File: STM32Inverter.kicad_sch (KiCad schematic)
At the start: 99 parts, among them J1 STLINK, J2 CURRENT SENSE, J5 UART, J6 INTERFACE, J7 POWER, J8 501571-2007, J9 RESOLVER, Q4 ST3422A, U1 STM32F303VCTx, U10 ULN2002, U11 LM393, U12 LM393, U4 74HCT00, U7 MCP2551-I-SN, Y3 CSTNE8M00GH5C000R0

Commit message: Review done
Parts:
- added JP1, JP2: ~, MEMS_Passive:R_0805_2012Metric_Jumper, symbol MEMS_Passive:SolderableJumper
- added unit 3 of U4
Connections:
- net GND: now also JP1.2, JP2.2, U4.10, U4.9
- net at J6.12, JP2.2: now also JP1.1
- net at J6.14, JP1.2: now also JP2.1
- no-connect marks 5 -> 53
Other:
- note removed: "CHECK NTC TEMP RANGE"
- note removed: "CHECK PINOUT"
- note removed: "Zrob Cos z VBUSEM !!!!"
- moved on the sheet: F3, JP1, JP2

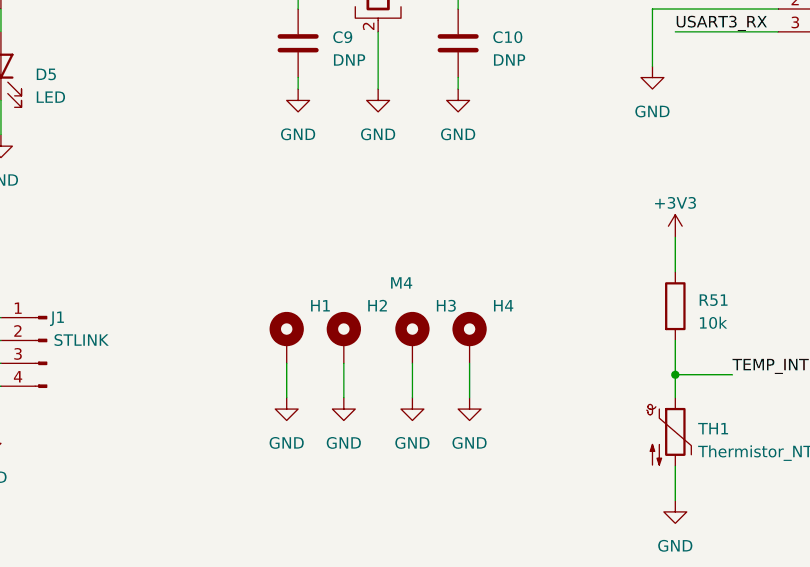
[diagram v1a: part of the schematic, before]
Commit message: change holes
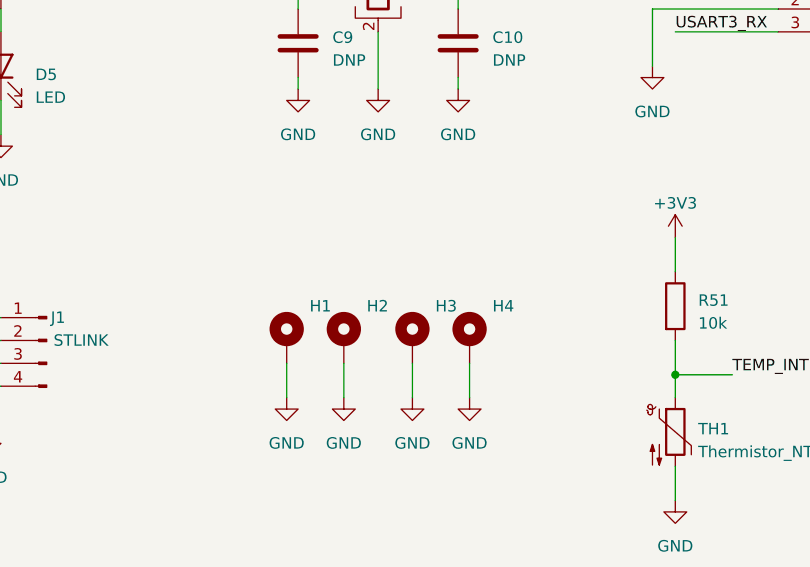
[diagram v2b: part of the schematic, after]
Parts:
- H1: value M4 -> MountingHole_Pad; footprint MountingHole:MountingHole_4.3mm_M4_ISO7380_Pad -> MountingHole:MountingHole_4.3mm_M4_Pad_Via
- H2, H3, H4: footprint MountingHole:MountingHole_4.3mm_M4_ISO7380_Pad -> MountingHole:MountingHole_4.3mm_M4_Pad_Via
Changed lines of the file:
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@@
       (effects (font (size 1.27 1.27)) (justify left) hide)
     )
-    (property "Footprint" "MountingHole:MountingHole_4.3mm_M4_ISO7380_Pad" (at 256.54 367.03 0)
+    (property "Footprint" "MountingHole:MountingHole_4.3mm_M4_Pad_Via" (at 256.54 367.03 0)
       (effects (font (size 1.27 1.27)) hide)
     )
@@
       (effects (font (size 1.27 1.27)) (justify left) hide)
     )
-    (property "Footprint" "MountingHole:MountingHole_4.3mm_M4_ISO7380_Pad" (at 250.19 367.03 0)
+    (property "Footprint" "MountingHole:MountingHole_4.3mm_M4_Pad_Via" (at 250.19 367.03 0)
       (effects (font (size 1.27 1.27)) hide)
     )
@@
       (effects (font (size 1.27 1.27)) (justify left) hide)
     )
-    (property "Footprint" "MountingHole:MountingHole_4.3mm_M4_ISO7380_Pad" (at 242.57 367.03 0)
+    (property "Footprint" "MountingHole:MountingHole_4.3mm_M4_Pad_Via" (at 242.57 367.03 0)
       (effects (font (size 1.27 1.27)) hide)
     )
@@
       (effects (font (size 1.27 1.27)) (justify left))
     )
-    (property "Value" "M4" (at 247.65 360.68 0)
-      (effects (font (size 1.27 1.27)) (justify left))
-    )
-    (property "Footprint" "MountingHole:MountingHole_4.3mm_M4_ISO7380_Pad" (at 236.22 367.03 0)
-      (effects (font (size 1.27 1.27)) hide)
-    )
+    (property "Value" "MountingHole_Pad" (at 240.03 360.68 0)
+      (effects (font (size 1.27 1.27)) (justify left) hide)
+    )
+    (property "Footprint" "MountingHole:MountingHole_4.3mm_M4_Pad_Via" (at 236.22 367.03 0)
+      (effects (font (size 1.27 1.27)) hide)
+    )

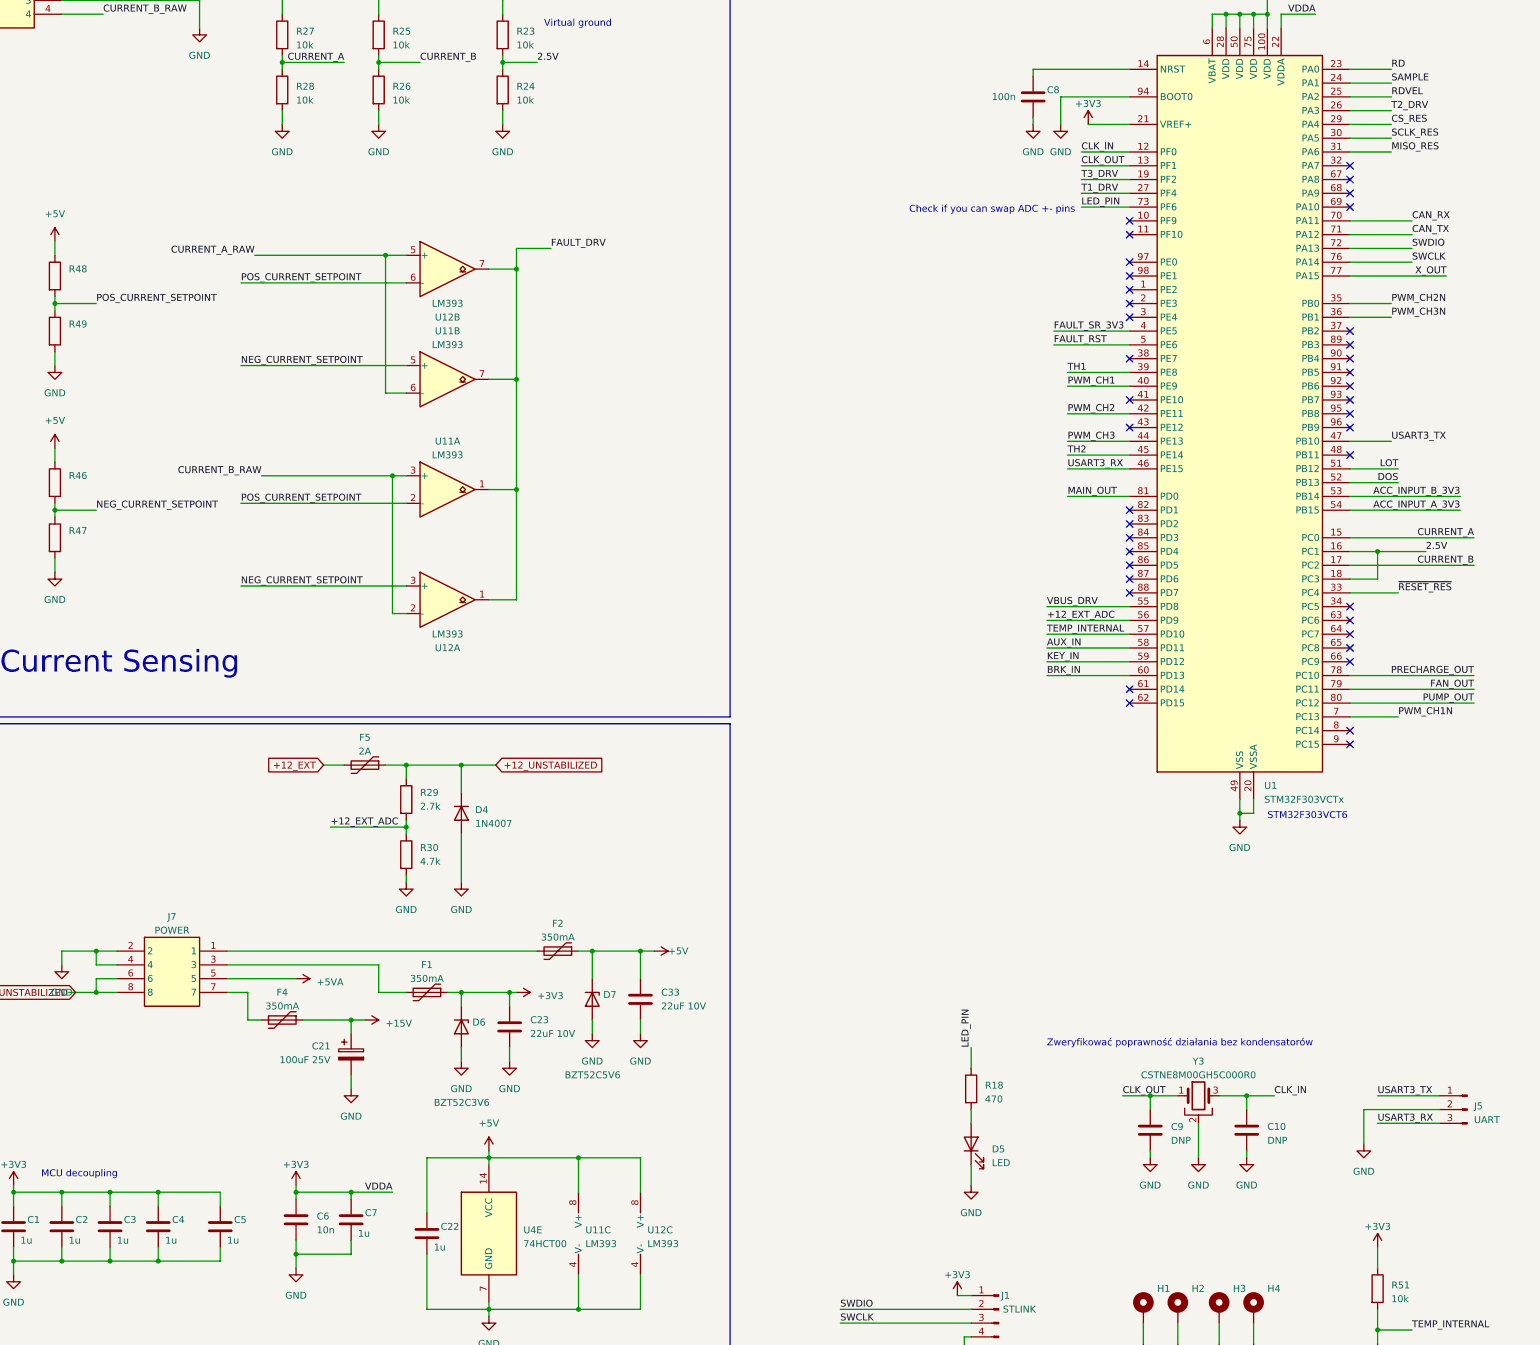
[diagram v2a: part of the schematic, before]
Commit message: Move T1-3 from ADC1 to ADC2\nNow ADC1 is used only for current measurment
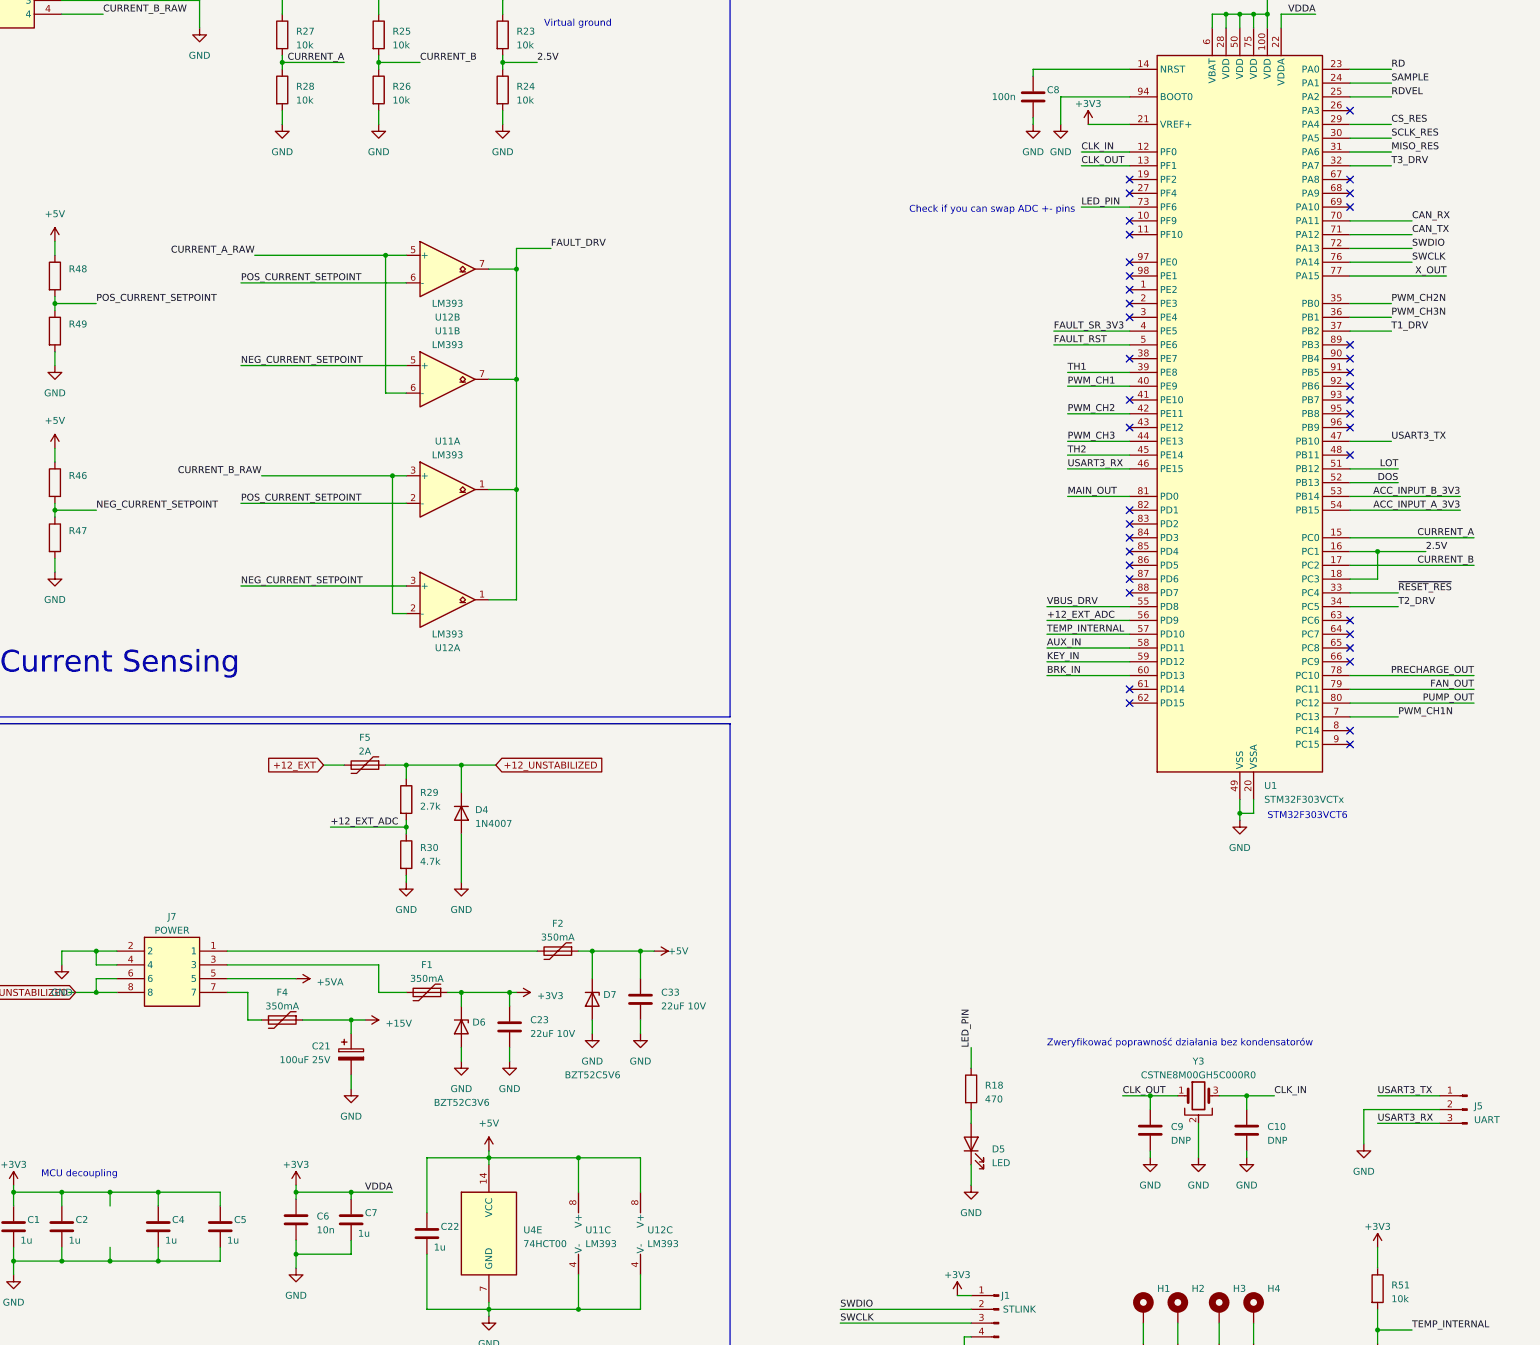
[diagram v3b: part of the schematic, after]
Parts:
- removed C3: 1u, Capacitor_SMD:C_0402_1005Metric_Pad0.74x0.62mm_HandSolder, symbol Device:C
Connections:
- net T1_DRV: now also U1.37 (PB2); no longer U1.27 (PF4)
- net T2_DRV: now also U1.34 (PC5); no longer U1.26 (PA3)
- net T3_DRV: now also U1.32 (PA7); no longer U1.19 (PF2)
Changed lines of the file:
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@@
   (no_connect (at 488.95 147.32))
   (no_connect (at 233.68 166.37))
-  (no_connect (at 274.32 156.21))
-  (no_connect (at 274.32 237.49))
   (no_connect (at 274.32 161.29))
-  (no_connect (at 274.32 186.69))
   (no_connect (at 274.32 260.35))
   (no_connect (at 233.68 229.87))
@@
   (no_connect (at 274.32 209.55))
   (no_connect (at 233.68 219.71))
+  (no_connect (at 274.32 146.05))
   (no_connect (at 274.32 240.03))
   (no_connect (at 274.32 189.23))
   (no_connect (at 233.68 222.25))
+  (no_connect (at 233.68 161.29))
   (no_connect (at 233.68 173.99))
   (no_connect (at 440.69 214.63))
@@
   (no_connect (at 511.81 147.32))
   (no_connect (at 236.22 58.42))
+  (no_connect (at 233.68 158.75))
   (no_connect (at 233.68 255.27))
   (no_connect (at 233.68 232.41))
@@
     (stroke (width 0) (type default))
   )
+  (wire (pts (xy 274.32 237.49) (xy 283.21 237.49))
+    (stroke (width 0) (type default))
+  )
   (wire (pts (xy 485.14 43.18) (xy 491.49 43.18))
     (stroke (width 0) (type default))
@@
     (stroke (width 0) (type default))
   )
+  (wire (pts (xy 274.32 186.69) (xy 281.94 186.69))
+    (stroke (width 0) (type default))
+  )
   (wire (pts (xy 274.32 168.91) (xy 285.75 168.91))
     (stroke (width 0) (type default))
@@
     (stroke (width 0) (type default))
   )
-  (wire (pts (xy 448.31 36.83) (xy 459.74 36.83))
+  (wire (pts (xy 274.32 156.21) (xy 281.94 156.21))
     (stroke (width 0) (type default))
   )
-  (wire (pts (xy 224.79 161.29) (xy 233.68 161.29))
+  (wire (pts (xy 448.31 36.83) (xy 459.74 36.83))
     (stroke (width 0) (type default))
   )
@@
     (stroke (width 0) (type default))
   )
-  (wire (pts (xy 281.94 146.05) (xy 274.32 146.05))
-    (stroke (width 0) (type default))
-  )
   (wire (pts (xy 168.91 72.39) (xy 168.91 69.85))
     (stroke (width 0) (type default))
@@
     (stroke (width 0) (type default))
   )
-  (wire (pts (xy 224.79 158.75) (xy 233.68 158.75))
-    (stroke (width 0) (type default))
-  )
   (wire (pts (xy 543.56 132.08) (xy 543.56 134.62))
     (stroke (width 0) (type default))
@@
     (effects (font (size 1.27 1.27)) (justify left bottom))
   )
-  (label "T3_DRV" (at 224.79 158.75 0) (fields_autoplaced)
+  (label "T3_DRV" (at 281.94 156.21 0) (fields_autoplaced)
     (effects (font (size 1.27 1.27)) (justify left bottom))
   )
@@
     (effects (font (size 1.27 1.27)) (justify left bottom))
   )
-  (label "T1_DRV" (at 224.79 161.29 0) (fields_autoplaced)
+  (label "T1_DRV" (at 281.94 186.69 0) (fields_autoplaced)
     (effects (font (size 1.27 1.27)) (justify left bottom))
   )
@@
     (effects (font (size 1.27 1.27)) (justify right bottom))
   )
-  (label "T2_DRV" (at 281.94 146.05 0) (fields_autoplaced)
+  (label "T2_DRV" (at 283.21 237.49 0) (fields_autoplaced)
     (effects (font (size 1.27 1.27)) (justify left bottom))
   )
@@
         )
       )
-    )
-  )
-  (symbol (lib_id "Device:C") (at 45.72 351.79 0) (unit 1)
-    (in_bom yes) (on_board yes) (dnp no)
-    (property "Reference" "C3" (at 48.26 350.52 0)
-      (effects (font (size 1.27 1.27)) (justify left))
-    )
-    (property "Value" "1u" (at 46.99 354.33 0)
-      (effects (font (size 1.27 1.27)) (justify left))
-    )
-    (property "Footprint" "Capacitor_SMD:C_0402_1005Metric_Pad0.74x0.62mm_HandSolder" (at 46.6852 355.6 0)
-      (effects (font (size 1.27 1.27)) hide)
-    )
-    (property "Datasheet" "~" (at 45.72 351.79 0)
-      (effects (font (size 1.27 1.27)) hide)
-    )
-    (property "LCSC" "C126521" (at 45.72 351.79 0)
-      (effects (font (size 1.27 1.27)) hide)
-    )
-    (pin "1")
-    (pin "2")
-    (instances
-      (project "STM32Inverter"
-        (path "/a3442e80-7eef-4b96-92a1-138eb3b79ccb"
-          (reference "C3") (unit 1)
-        )
-      )
